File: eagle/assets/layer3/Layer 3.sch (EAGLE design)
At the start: 84 parts, among them Q2 AO3402, X1 SM06B-SRSS-TB, Y1 8MHz

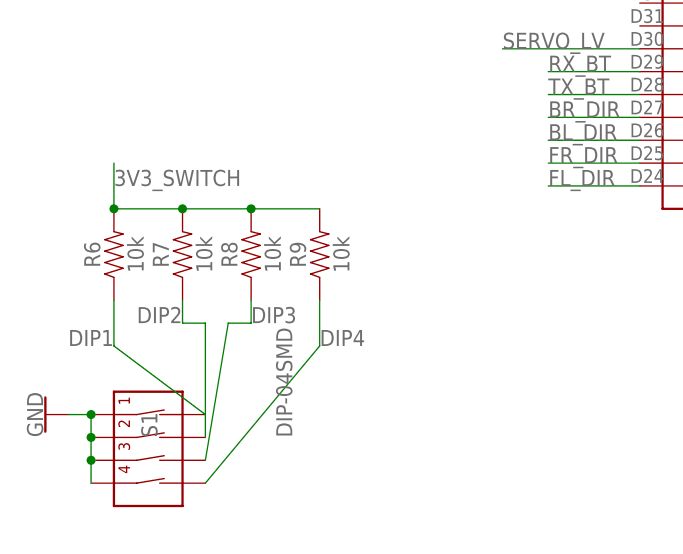
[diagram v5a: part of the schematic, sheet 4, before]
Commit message: added teensy 4 lbr
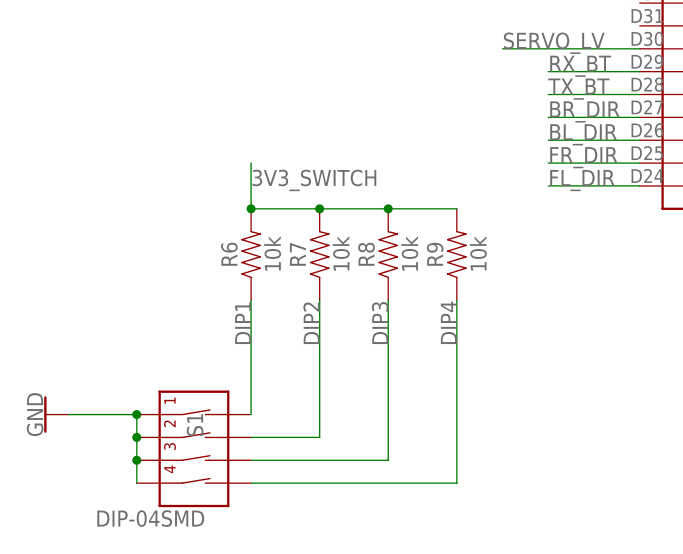
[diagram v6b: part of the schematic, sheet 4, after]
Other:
- moved on the sheet: R6, R7, R8, R9, S1
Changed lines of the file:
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@@
 <attribute name="VALUE" x="205.74" y="121.666" size="1.778" layer="96" align="top-center"/>
 </instance>
-<instance part="S1" gate="G$1" x="30.48" y="38.1" smashed="yes">
-<attribute name="NAME" x="30.226" y="38.1" size="1.778" layer="95" font="vector" rot="R90"/>
-<attribute name="VALUE" x="43.434" y="38.1" size="1.778" layer="96" font="vector" rot="R90" align="top-left"/>
+<instance part="S1" gate="G$1" x="35.56" y="38.1" smashed="yes">
+<attribute name="NAME" x="35.306" y="38.1" size="1.778" layer="95" font="vector" rot="R90"/>
+<attribute name="VALUE" x="35.56" y="28.194" size="1.778" layer="96" font="vector" rot="R180" align="top-left"/>
 </instance>
 <instance part="GND38" gate="1" x="17.78" y="40.64" smashed="yes" rot="R270">
 <attribute name="VALUE" x="17.526" y="40.64" size="1.778" layer="96" rot="R270" align="top-center"/>
 </instance>
-<instance part="R6" gate="G$1" x="25.4" y="58.42" smashed="yes" rot="R90">
-<attribute name="NAME" x="23.876" y="58.42" size="1.778" layer="95" font="vector" rot="R90" align="bottom-center"/>
-<attribute name="VALUE" x="26.924" y="58.42" size="1.778" layer="96" font="vector" rot="R90" align="top-center"/>
-</instance>
-<instance part="R7" gate="G$1" x="33.02" y="58.42" smashed="yes" rot="R90">
-<attribute name="NAME" x="31.496" y="58.42" size="1.778" layer="95" font="vector" rot="R90" align="bottom-center"/>
-<attribute name="VALUE" x="34.544" y="58.42" size="1.778" layer="96" font="vector" rot="R90" align="top-center"/>
-</instance>
-<instance part="R8" gate="G$1" x="40.64" y="58.42" smashed="yes" rot="R90">
+<instance part="R6" gate="G$1" x="40.64" y="58.42" smashed="yes" rot="R90">
 <attribute name="NAME" x="39.116" y="58.42" size="1.778" layer="95" font="vector" rot="R90" align="bottom-center"/>
 <attribute name="VALUE" x="42.164" y="58.42" size="1.778" layer="96" font="vector" rot="R90" align="top-center"/>
 </instance>
-<instance part="R9" gate="G$1" x="48.26" y="58.42" smashed="yes" rot="R90">
+<instance part="R7" gate="G$1" x="48.26" y="58.42" smashed="yes" rot="R90">
 <attribute name="NAME" x="46.736" y="58.42" size="1.778" layer="95" font="vector" rot="R90" align="bottom-center"/>
 <attribute name="VALUE" x="49.784" y="58.42" size="1.778" layer="96" font="vector" rot="R90" align="top-center"/>
+</instance>
+<instance part="R8" gate="G$1" x="55.88" y="58.42" smashed="yes" rot="R90">
+<attribute name="NAME" x="54.356" y="58.42" size="1.778" layer="95" font="vector" rot="R90" align="bottom-center"/>
+<attribute name="VALUE" x="57.404" y="58.42" size="1.778" layer="96" font="vector" rot="R90" align="top-center"/>
+</instance>
+<instance part="R9" gate="G$1" x="63.5" y="58.42" smashed="yes" rot="R90">
+<attribute name="NAME" x="61.976" y="58.42" size="1.778" layer="95" font="vector" rot="R90" align="bottom-center"/>
+<attribute name="VALUE" x="65.024" y="58.42" size="1.778" layer="96" font="vector" rot="R90" align="top-center"/>
 </instance>
 <instance part="BLUETOOTH" gate="G$1" x="220.98" y="96.52" smashed="yes">
@@
 <pinref part="S1" gate="G$1" pin="4B"/>
 <pinref part="S1" gate="G$1" pin="1B"/>
-<wire x1="22.86" y1="33.02" x2="22.86" y2="35.56" width="0.1524" layer="91"/>
+<wire x1="27.94" y1="33.02" x2="27.94" y2="35.56" width="0.1524" layer="91"/>
 <pinref part="S1" gate="G$1" pin="2B"/>
-<wire x1="22.86" y1="35.56" x2="22.86" y2="38.1" width="0.1524" layer="91"/>
-<wire x1="22.86" y1="38.1" x2="22.86" y2="40.64" width="0.1524" layer="91"/>
-<junction x="22.86" y="38.1"/>
+<wire x1="27.94" y1="35.56" x2="27.94" y2="38.1" width="0.1524" layer="91"/>
+<wire x1="27.94" y1="38.1" x2="27.94" y2="40.64" width="0.1524" layer="91"/>
+<junction x="27.94" y="38.1"/>
 <pinref part="S1" gate="G$1" pin="3B"/>
-<junction x="22.86" y="35.56"/>
+<junction x="27.94" y="35.56"/>
 <pinref part="GND38" gate="1" pin="GND"/>
-<wire x1="22.86" y1="40.64" x2="20.32" y2="40.64" width="0.1524" layer="91"/>
-<junction x="22.86" y="40.64"/>
+<wire x1="27.94" y1="40.64" x2="20.32" y2="40.64" width="0.1524" layer="91"/>
+<junction x="27.94" y="40.64"/>
 </segment>
 <segment>
@@
 <segment>
 <pinref part="S1" gate="G$1" pin="1A"/>
-<wire x1="35.56" y1="40.64" x2="25.4" y2="48.26" width="0.1524" layer="91"/>
+<wire x1="40.64" y1="40.64" x2="40.64" y2="53.34" width="0.1524" layer="91"/>
 <pinref part="R6" gate="G$1" pin="1"/>
-<wire x1="25.4" y1="48.26" x2="25.4" y2="53.34" width="0.1524" layer="91"/>
-<label x="20.32" y="48.26" size="1.778" layer="95"/>
+<label x="40.64" y="48.26" size="1.778" layer="95" rot="R90"/>
 </segment>
 <segment>
@@
 <segment>
 <pinref part="S1" gate="G$1" pin="2A"/>
-<wire x1="35.56" y1="38.1" x2="35.56" y2="50.8" width="0.1524" layer="91"/>
-<wire x1="35.56" y1="50.8" x2="33.02" y2="50.8" width="0.1524" layer="91"/>
+<wire x1="40.64" y1="38.1" x2="48.26" y2="38.1" width="0.1524" layer="91"/>
 <pinref part="R7" gate="G$1" pin="1"/>
-<wire x1="33.02" y1="50.8" x2="33.02" y2="53.34" width="0.1524" layer="91"/>
-<label x="27.94" y="50.8" size="1.778" layer="95"/>
+<wire x1="48.26" y1="38.1" x2="48.26" y2="53.34" width="0.1524" layer="91"/>
+<label x="48.26" y="48.26" size="1.778" layer="95" rot="R90"/>
 </segment>
 <segment>
@@
 <segment>
 <pinref part="S1" gate="G$1" pin="3A"/>
-<wire x1="35.56" y1="35.56" x2="38.1" y2="50.8" width="0.1524" layer="91"/>
-<wire x1="38.1" y1="50.8" x2="40.64" y2="50.8" width="0.1524" layer="91"/>
+<wire x1="40.64" y1="35.56" x2="55.88" y2="35.56" width="0.1524" layer="91"/>
+<wire x1="55.88" y1="35.56" x2="55.88" y2="53.34" width="0.1524" layer="91"/>
 <pinref part="R8" gate="G$1" pin="1"/>
-<wire x1="40.64" y1="50.8" x2="40.64" y2="53.34" width="0.1524" layer="91"/>
-<label x="40.64" y="50.8" size="1.778" layer="95"/>
+<label x="55.88" y="48.26" size="1.778" layer="95" rot="R90"/>
 </segment>
 <segment>
@@
 <segment>
 <pinref part="S1" gate="G$1" pin="4A"/>
-<wire x1="35.56" y1="33.02" x2="48.26" y2="48.26" width="0.1524" layer="91"/>
+<wire x1="40.64" y1="33.02" x2="63.5" y2="33.02" width="0.1524" layer="91"/>
 <pinref part="R9" gate="G$1" pin="1"/>
-<wire x1="48.26" y1="48.26" x2="48.26" y2="53.34" width="0.1524" layer="91"/>
-<label x="48.26" y="48.26" size="1.778" layer="95"/>
+<wire x1="63.5" y1="33.02" x2="63.5" y2="53.34" width="0.1524" layer="91"/>
+<label x="63.5" y="48.26" size="1.778" layer="95" rot="R90"/>
 </segment>
 <segment>
@@
 <pinref part="R6" gate="G$1" pin="2"/>
 <pinref part="R9" gate="G$1" pin="2"/>
-<wire x1="25.4" y1="63.5" x2="33.02" y2="63.5" width="0.1524" layer="91"/>
+<wire x1="40.64" y1="63.5" x2="48.26" y2="63.5" width="0.1524" layer="91"/>
 <pinref part="R7" gate="G$1" pin="2"/>
-<wire x1="33.02" y1="63.5" x2="40.64" y2="63.5" width="0.1524" layer="91"/>
-<junction x="33.02" y="63.5"/>
+<wire x1="48.26" y1="63.5" x2="55.88" y2="63.5" width="0.1524" layer="91"/>
+<junction x="48.26" y="63.5"/>
 <pinref part="R8" gate="G$1" pin="2"/>
-<wire x1="40.64" y1="63.5" x2="48.26" y2="63.5" width="0.1524" layer="91"/>
+<wire x1="55.88" y1="63.5" x2="63.5" y2="63.5" width="0.1524" layer="91"/>
+<junction x="55.88" y="63.5"/>
+<wire x1="40.64" y1="63.5" x2="40.64" y2="68.58" width="0.1524" layer="91"/>
 <junction x="40.64" y="63.5"/>
-<wire x1="25.4" y1="63.5" x2="25.4" y2="68.58" width="0.1524" layer="91"/>
-<junction x="25.4" y="63.5"/>
-<label x="25.4" y="66.04" size="1.778" layer="95"/>
-</segment>
-</net>
+<label x="40.64" y="66.04" size="1.778" layer="95"/>
+</segment>
+</net>

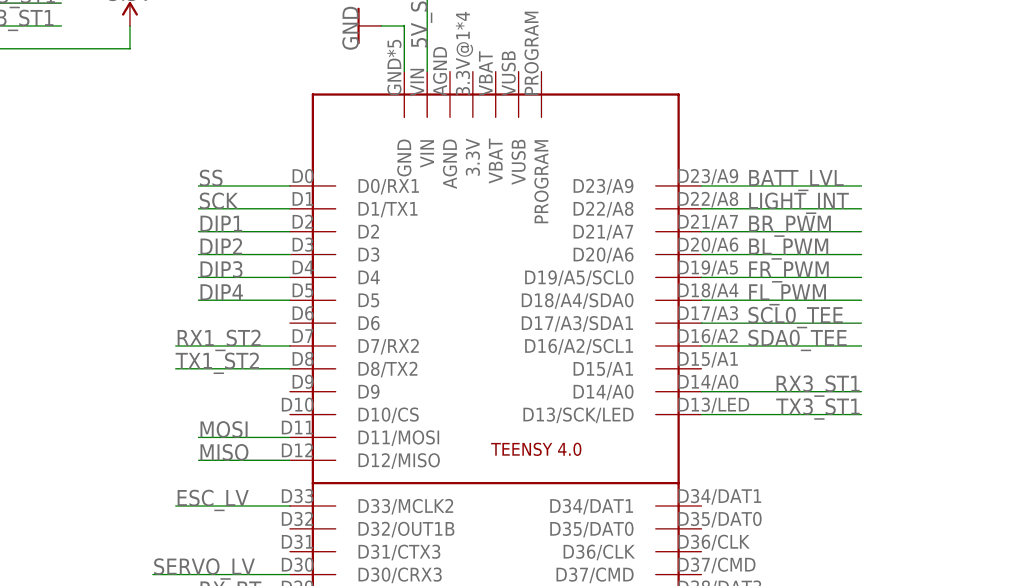
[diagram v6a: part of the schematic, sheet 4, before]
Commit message: Edited teensy 4 pin out
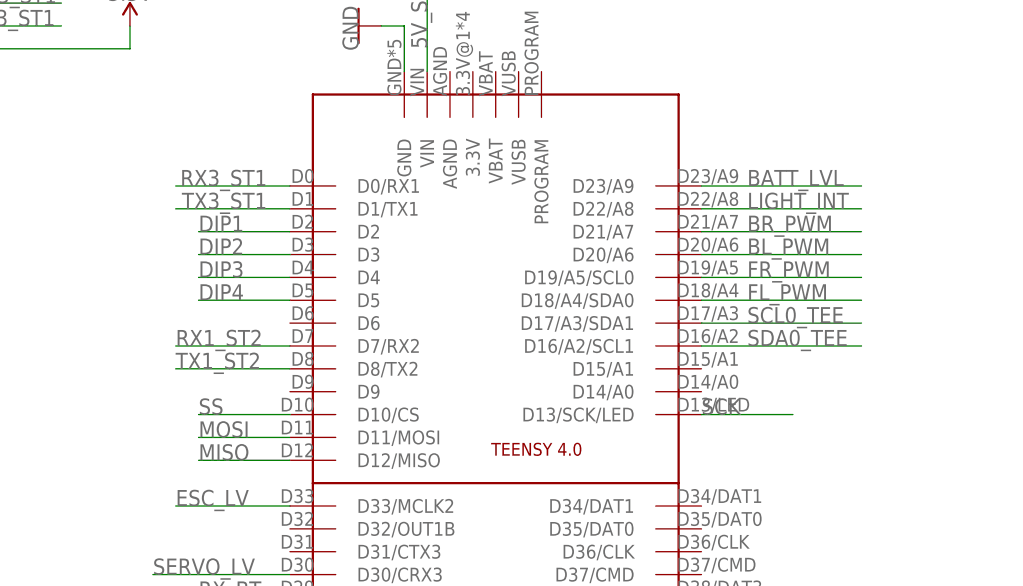
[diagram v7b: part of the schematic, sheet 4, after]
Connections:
- net RX3_ST1: now also TEENSY4.D0/RX1; no longer TEENSY4.D14/A0
- net SCK: now also TEENSY4.D13/SCK/LED; no longer TEENSY4.D1/TX1
- net SS: now also TEENSY4.D10/CS; no longer TEENSY4.D0/RX1
- net TX3_ST1: now also TEENSY4.D1/TX1; no longer TEENSY4.D13/SCK/LED
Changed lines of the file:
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@@
 </segment>
 <segment>
-<wire x1="129.54" y1="101.6" x2="147.32" y2="101.6" width="0.1524" layer="91"/>
-<label x="147.32" y="103.378" size="1.778" layer="95" rot="R180"/>
-<pinref part="TEENSY4" gate="G$1" pin="D14/A0"/>
+<wire x1="71.12" y1="124.46" x2="83.82" y2="124.46" width="0.1524" layer="91"/>
+<label x="81.28" y="126.238" size="1.778" layer="95" rot="R180"/>
+<pinref part="TEENSY4" gate="G$1" pin="D0/RX1"/>
 </segment>
 </net>
@@
 </segment>
 <segment>
-<wire x1="129.54" y1="99.06" x2="147.32" y2="99.06" width="0.1524" layer="91"/>
-<label x="147.32" y="100.838" size="1.778" layer="95" rot="R180"/>
-<pinref part="TEENSY4" gate="G$1" pin="D13/SCK/LED"/>
+<wire x1="71.12" y1="121.92" x2="83.82" y2="121.92" width="0.1524" layer="91"/>
+<label x="81.28" y="123.698" size="1.778" layer="95" rot="R180"/>
+<pinref part="TEENSY4" gate="G$1" pin="D1/TX1"/>
 </segment>
 </net>
@@
 </segment>
 <segment>
-<pinref part="TEENSY4" gate="G$1" pin="D1/TX1"/>
-<wire x1="83.82" y1="121.92" x2="73.66" y2="121.92" width="0.1524" layer="91"/>
-<label x="73.66" y="121.92" size="1.778" layer="95"/>
+<wire x1="139.7" y1="99.06" x2="129.54" y2="99.06" width="0.1524" layer="91"/>
+<label x="129.54" y="99.06" size="1.778" layer="95"/>
+<pinref part="TEENSY4" gate="G$1" pin="D13/SCK/LED"/>
 </segment>
 </net>
@@
 </segment>
 <segment>
-<pinref part="TEENSY4" gate="G$1" pin="D0/RX1"/>
-<wire x1="83.82" y1="124.46" x2="73.66" y2="124.46" width="0.1524" layer="91"/>
-<label x="73.66" y="124.46" size="1.778" layer="95"/>
-</segment>
-</net>
+<wire x1="83.82" y1="99.06" x2="73.66" y2="99.06" width="0.1524" layer="91"/>
+<label x="73.66" y="99.06" size="1.778" layer="95"/>
+<pinref part="TEENSY4" gate="G$1" pin="D10/CS"/>
+</segment>
+</net>

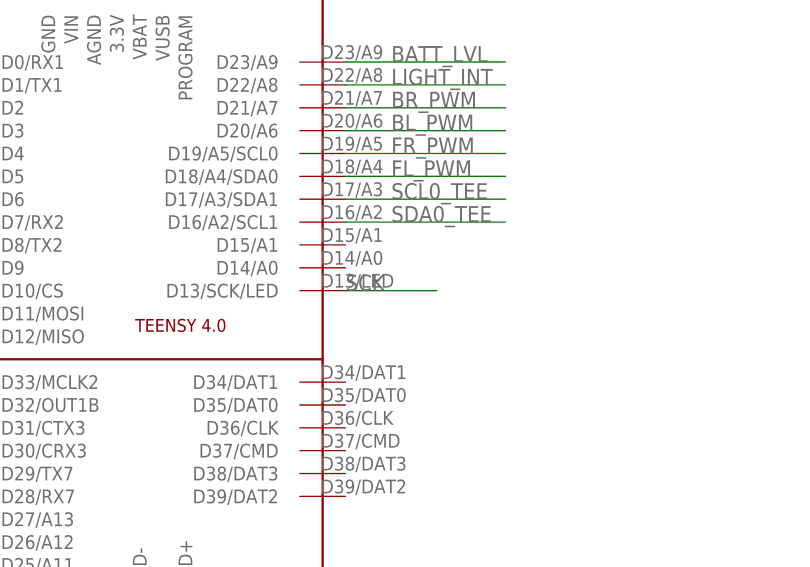
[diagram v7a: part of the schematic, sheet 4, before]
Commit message: Edited teensy 4 pin out
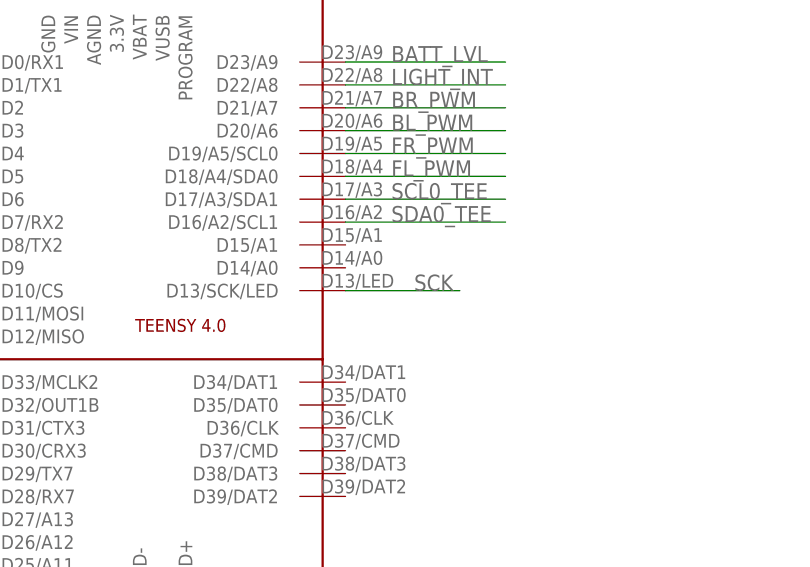
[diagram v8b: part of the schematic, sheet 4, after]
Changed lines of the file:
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@@
 </segment>
 <segment>
-<wire x1="139.7" y1="99.06" x2="129.54" y2="99.06" width="0.1524" layer="91"/>
-<label x="129.54" y="99.06" size="1.778" layer="95"/>
+<wire x1="142.24" y1="99.06" x2="129.54" y2="99.06" width="0.1524" layer="91"/>
+<label x="137.16" y="99.06" size="1.778" layer="95"/>
 <pinref part="TEENSY4" gate="G$1" pin="D13/SCK/LED"/>
 </segment>
